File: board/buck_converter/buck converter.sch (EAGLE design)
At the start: 8 parts, among them IC1 TPS84621

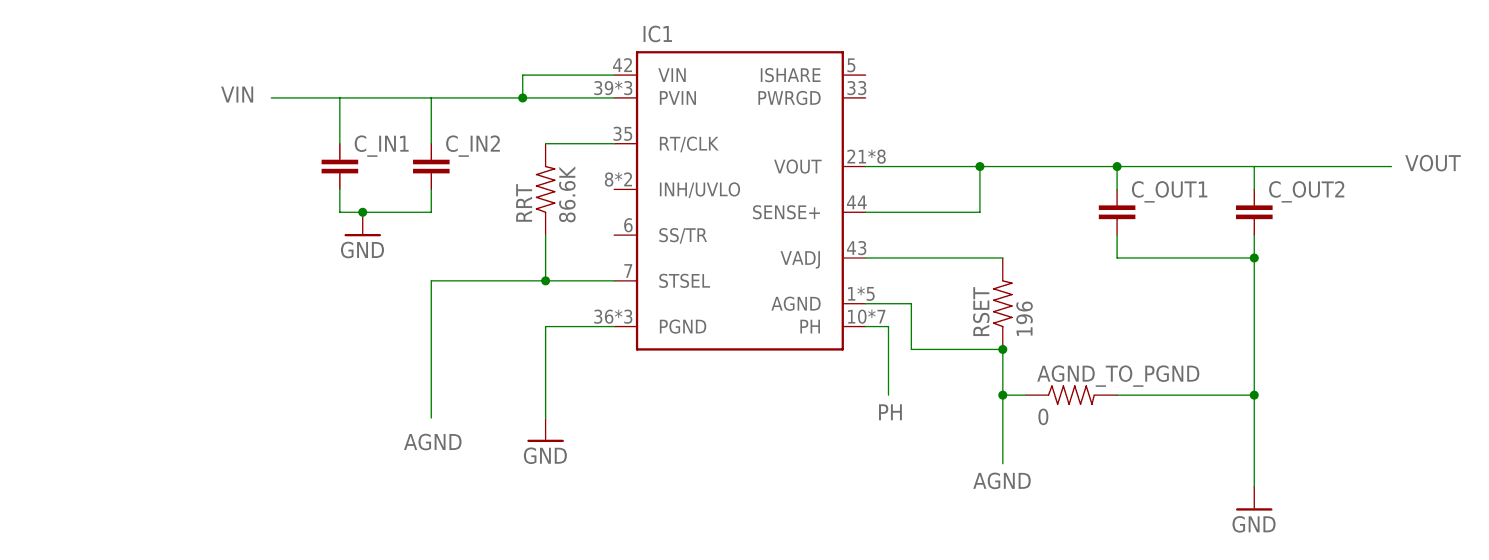
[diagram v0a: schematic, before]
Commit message: Some routing polygons added.
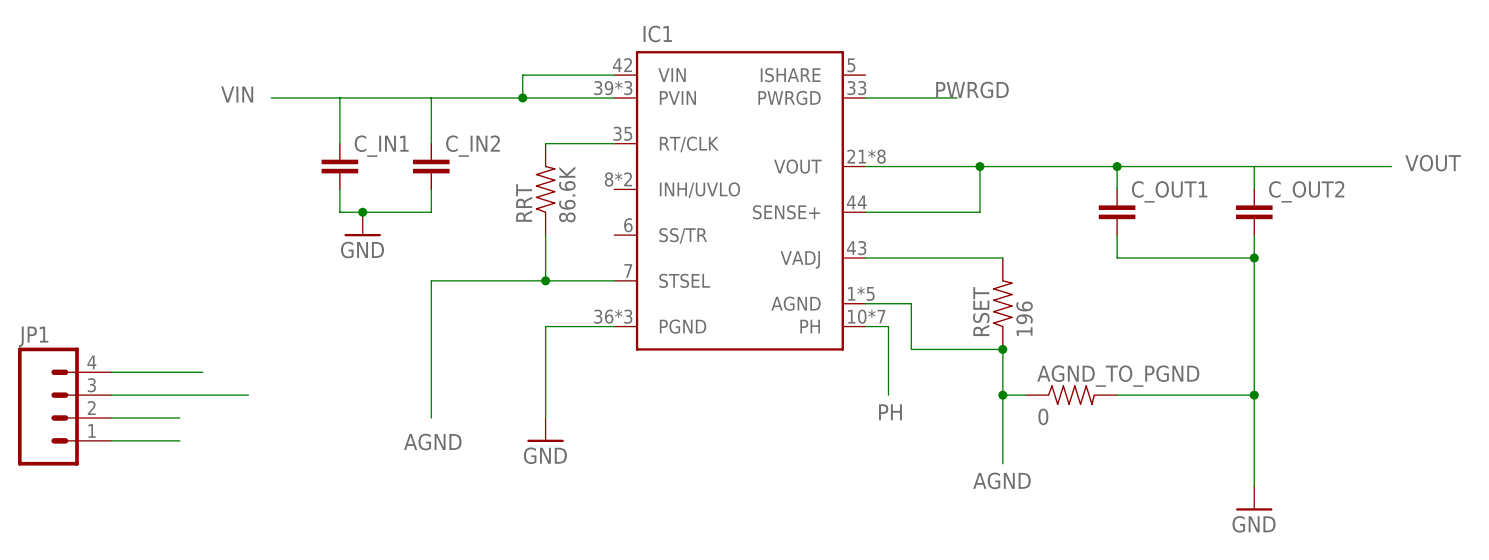
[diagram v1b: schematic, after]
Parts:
- added JP1: (no value), SparkFun-Connectors:M04PTH
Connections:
- new net PWRGD: IC1.PWRGD, JP1.4
- net GND: now also JP1.2
- net VIN: now also JP1.1
- net VOUT: now also JP1.3
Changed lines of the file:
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@@
 <part name="RSET" library="biomimetic" deviceset="RESISTOR" device="0402-RES" value="196"/>
 <part name="RRT" library="biomimetic" deviceset="RESISTOR" device="0402-RES" value="86.6K"/>
+<part name="JP1" library="SparkFun-Connectors" deviceset="M04" device="PTH"/>
 </parts>
 <sheets>
@@
 <instance part="RSET" gate="G$1" x="142.24" y="101.6" rot="R90"/>
 <instance part="RRT" gate="G$1" x="91.44" y="114.3" rot="R90"/>
+<instance part="JP1" gate="G$1" x="38.1" y="88.9"/>
 </instances>
 <busses>
@@
 <wire x1="139.7" y1="111.76" x2="139.7" y2="116.84" width="0.1524" layer="91"/>
 <junction x="139.7" y="116.84"/>
+</segment>
+<segment>
+<wire x1="43.18" y1="91.44" x2="58.42" y2="91.44" width="0.1524" layer="91"/>
+<pinref part="JP1" gate="G$1" pin="3"/>
 </segment>
 </net>
@@
 <pinref part="GND1" gate="1" pin="GND"/>
 <junction x="71.12" y="111.76"/>
+</segment>
+<segment>
+<wire x1="50.8" y1="88.9" x2="43.18" y2="88.9" width="0.1524" layer="91"/>
+<pinref part="JP1" gate="G$1" pin="2"/>
 </segment>
 </net>
@@
 <wire x1="78.74" y1="119.38" x2="78.74" y2="124.46" width="0.1524" layer="91"/>
 </segment>
+<segment>
+<wire x1="50.8" y1="86.36" x2="43.18" y2="86.36" width="0.1524" layer="91"/>
+<pinref part="JP1" gate="G$1" pin="1"/>
+</segment>
 </net>
 <net name="N$1" class="0">
@@
 </segment>
 </net>
+<net name="PWRGD" class="0">
+<segment>
+<pinref part="IC1" gate="G$1" pin="PWRGD"/>
+<wire x1="127" y1="124.46" x2="137.16" y2="124.46" width="0.1524" layer="91"/>
+<label x="134.62" y="124.46" size="1.778" layer="95"/>
+</segment>
+<segment>
+<wire x1="43.18" y1="93.98" x2="53.34" y2="93.98" width="0.1524" layer="91"/>
+<pinref part="JP1" gate="G$1" pin="4"/>
+</segment>
+</net>
